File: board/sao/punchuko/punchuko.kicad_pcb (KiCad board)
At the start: 2 copper layers, 48.7 x 43.5 mm, 4 parts

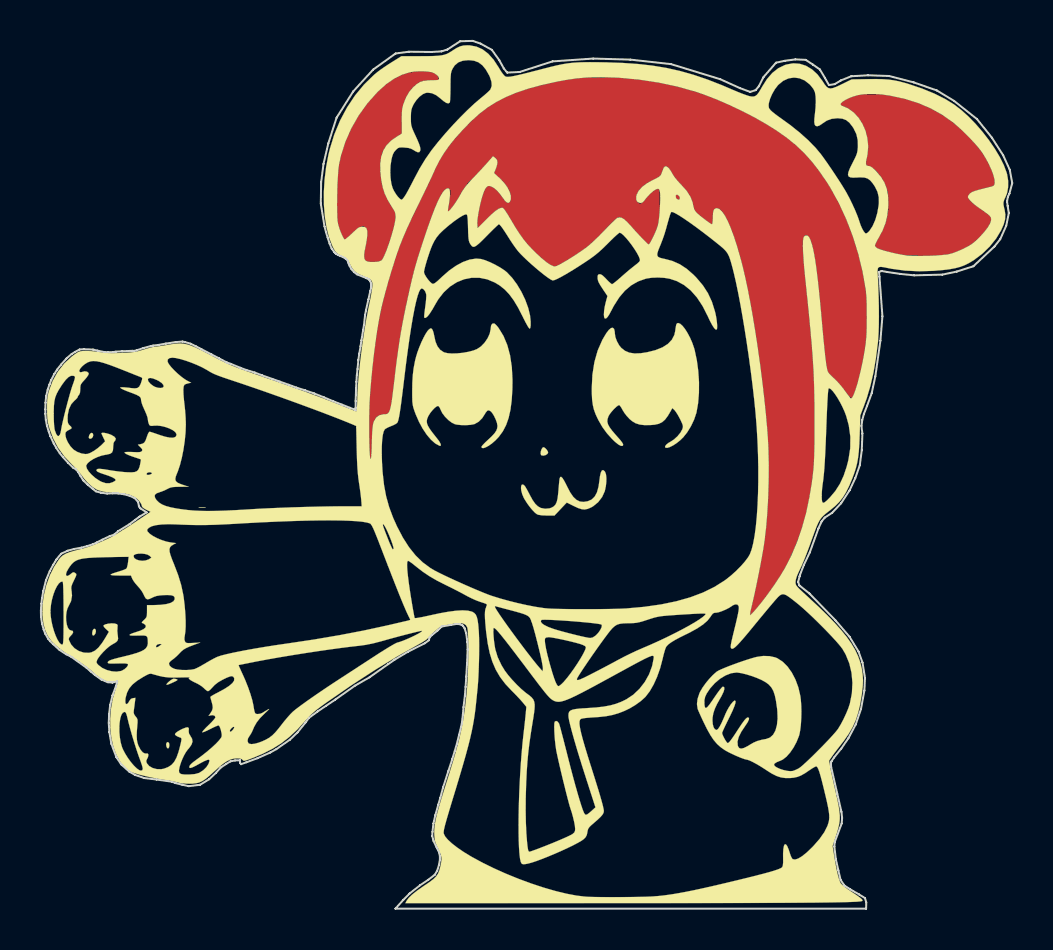
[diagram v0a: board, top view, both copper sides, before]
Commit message: wired power and LED matrix
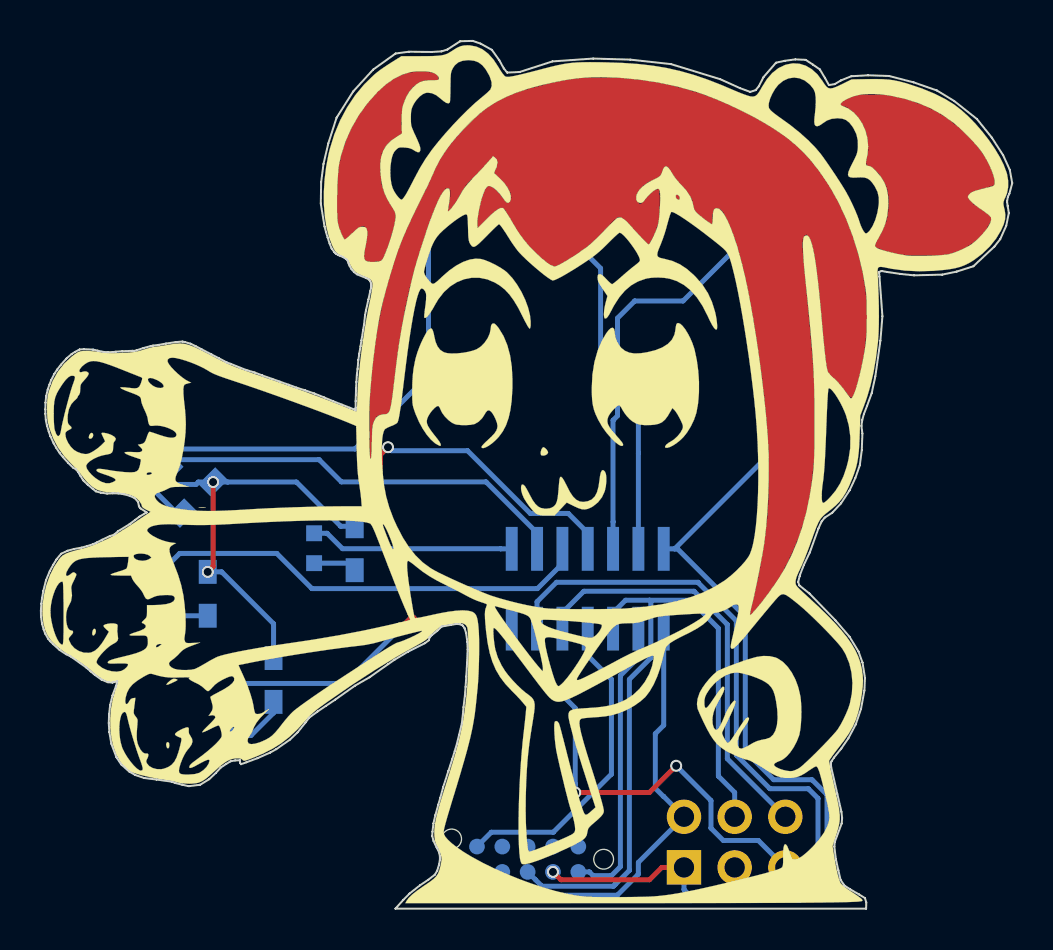
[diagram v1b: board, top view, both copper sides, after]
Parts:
- removed the G*** at (76.1, 48.9) (x4)
- added D0: LED, LEDs:LED_0603, B.Cu at (73.7, 36.3)
- added D1: LED, LEDs:LED_0603, B.Cu at (90.2, 37.3)
- added D2: LED, LEDs:LED_0603, B.Cu at (62.0, 64.8)
- added D3: LED, LEDs:LED_0603, B.Cu at (58.2, 58.7)
- added D4: LED, LEDs:LED_0603, B.Cu at (58.2, 52.6)
- added D5: LED, LEDs:LED_0603, B.Cu at (65.8, 56.1)
- added G*** (x4): LOGO, LOGO, F.Cu at (76.1, 48.9)
- added G***: LOGO, punchuko:GRANTSIG10X10, B.Cu at (65.9, 52.4)
- added G***: LOGO, punchuko:finger, F.Cu at (104.4, 54.1)
- added IC1: ATTINY20-X, punchuko:ATTINY20_SOIC-14, B.Cu at (79.5, 58.2)
- added J1: PROG, punchuko:TC2050-All_Holes, B.Cu at (76.5, 71.7)
- added P1: SAO_PLUG, Socket_Strips:Socket_Strip_Straight_2x03, B.Cu at (84.3, 72.1)
- added R1: R, Resistors_SMD:R_0603_HandSoldering, B.Cu at (67.8, 56.1)
- added R2: R, Resistors_SMD:R_0603_HandSoldering, B.Cu at (59.9, 53.6)
- added R3: R, Resistors_SMD:R_0603_HandSoldering, B.Cu at (60.5, 58.4)
- added R4: R, Resistors_SMD:R_0603_HandSoldering, B.Cu at (63.8, 62.7)
- added R5: R, Resistors_SMD:R_0603_HandSoldering, B.Cu at (89.2, 39.1)
- added R6: R, Resistors_SMD:R_0603_HandSoldering, B.Cu at (75.4, 37.3)
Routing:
- net GND: track 0.00 -> 130.3 mm, vias 0 -> 3
- net /SDA/TPIDATA: track 0.00 -> 36.5 mm
- net Net-(D2-Pad2): track 0.00 -> 33.0 mm, vias 0 -> 2
- net /SCL: track 0.00 -> 33.0 mm
- net Net-(D0-Pad2): track 0.00 -> 24.7 mm, vias 0 -> 2
- net /GPIO2: track 0.00 -> 24.3 mm, vias 0 -> 2
- net Net-(D1-Pad2): track 0.00 -> 24.2 mm
- net Net-(D3-Pad2): track 0.00 -> 23.1 mm
- net +3V3: track 0.00 -> 21.8 mm
- net /GPIO1: track 0.00 -> 21.0 mm
- net Net-(D4-Pad2): track 0.00 -> 20.7 mm
- net /RESET: track 0.00 -> 16.0 mm
- net /TPICLK: track 0.00 -> 14.7 mm
- net Net-(D5-Pad2): track 0.00 -> 10.2 mm
- net Net-(D2-Pad1): track 0.00 -> 2.80 mm
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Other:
- board text added: "JLCJLCJLCJLC"
- board text added: "fuck you takeshobo!"
